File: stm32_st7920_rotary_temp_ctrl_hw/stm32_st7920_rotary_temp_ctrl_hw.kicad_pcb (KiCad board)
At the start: 2 copper layers, 100 x 100 mm, 177 parts, among them J1 Conn_01x02, J2 CONN_01X04, J3 USB_OTG, J4 CONN_01X04, J5 Conn_01x05, J7 Conn_01x03, J8 Conn_01x02, J9 Conn_01x06, Q1 C1815, Q10 C1815, Q11 IRF3205, Q12 ME15N10, Q13 ME15N10, Q14 ME15N10, Q15 ME15N10, Q2 C1815, Q3 C1815, Q4 C1815, Q5 C1815, Q6 A1015, Q7 C1815, Q8 C1815, Q9 C1815, SW1 SW_Push, SW2 SW_Push, SW3 SW_Push, SW4 SW_Push, U1 ASM1117, U10 24LC64, U2 MC34063, U3 MAX485, U4 STM32F103C8, U5 PC817, U6 74HC245, U7 PC817, U8 PC817, U9 PC817, Y1 Crystal, Y2 Crystal_GND3

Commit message: Delete block buton, Modify block connecter, Modify Block Power input, Update ALL footprint
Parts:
- removed C35, C36: 100nF, Capacitors_SMD:C_0805_HandSoldering
- removed C37: 100nF, Capacitor_SMD:C_0805_2012Metric_Pad1.15x1.40mm_HandSolder
- removed C38: 10uF, Capacitor_SMD:C_1206_3216Metric_Pad1.42x1.75mm_HandSolder
- removed D14, D15: D_Zener, nhantt-kicad-lib:SOD-80
- removed D16: SS54, nhantt-kicad-lib:D_SMB_Handsoldering
- removed D17, D18, D19, D20: FR107, nhantt-kicad-lib:D_SMA_Standard
- removed D21: TVS, nhantt-kicad-lib:D_SMA_Standard
- removed DHT1: DHT11, nhantt-kicad-lib:DHT11
- removed IoT-ETech: Val**, nhantt-kicad-lib:logo
- removed IoT-ETech: Val**, nhantt-kicad-lib:logo-Miror
- removed the J1 at (94.0, 63.5)
- removed J3: USB_OTG, nhantt-kicad-lib:USB_Micro-B
- removed J4: CONN_01X04, nhantt-kicad-lib:Header-4pin-2.54
- removed J7: Conn_01x03, nhantt-kicad-lib:Header-3pin-2.54
- removed LCD_ST7920: ST7920, nhantt-kicad-lib:ST7920
- removed Q10: C1815, nhantt-kicad-lib:SOT-23
- removed Q11: IRF3205, nhantt-kicad-lib:TO-263-2Lead
- removed Q12, Q13, Q14, Q15: ME15N10, nhantt-kicad-lib:TO-252-2
- removed R42: 1k, Resistors_SMD:R_0805_HandSoldering
- removed R43, R45, R46, R47, R48, R49, R50, R51, R52, R53: 2.2k, Resistors_SMD:R_0805_HandSoldering
- removed R44, R54, R55, R56, R57, R58, R59, R60, R61, R62: 10k, Resistors_SMD:R_0805_HandSoldering
- removed R63, R64, R65, R66, R67: 10R, Resistors_SMD:R_0805_HandSoldering
- removed SW1, SW2, SW3, SW4: SW_Push, Buttons_Switches_THT:SW_PUSH-12mm_Wuerth-430476085716
- removed U10: 24LC64, nhantt-kicad-lib:SOIC-8_3.9x4.9mm_Pitch1.27mm
- removed U6: 74HC245, Package_SO:TSSOP-20_4.4x6.5mm_P0.65mm
- removed U7, U8, U9: PC817, nhantt-kicad-lib:Optocoupler_SMD
- added F2: Fuse, Fuse:Fuse_1812_4532Metric_Pad1.30x3.40mm_HandSolder, F.Cu at (262.1, 94.8)
- added F3: Fuse, Fuse:Fuse_1812_4532Metric_Pad1.30x3.40mm_HandSolder, F.Cu at (262.1, 99.7)
- added H1: ~, Lib_Hien:KF142_9P_5.08, F.Cu at (258.1, 51.1)
- added H2: ~, Lib_Hien:KF142_9P_5.08, F.Cu at (258.1, 66.5)
- added IC1: MAX6675, Lib_Hien:MAX6675, F.Cu at (287.9, 106.0)
- added J1: USB_C_Receptacle_USB2.0, Connector_USB:USB_C_Receptacle_GCT_USB4105-xx-A_16P_TopMnt_Horizontal, F.Cu at (277.6, 106.7)
- added J1: Conn_01x02, nhantt-kicad-lib:TerminalBlock_WAGO-236_2Stift_R5mm_2pol, B.Cu at (-111.3, 64.2)
- added L3: L_Small, Resistor_SMD:R_0805_2012Metric_Pad1.20x1.40mm_HandSolder, F.Cu at (299.8, 33.0)
- added R35: 2.2k, Resistor_SMD:R_0805_2012Metric_Pad1.20x1.40mm_HandSolder, F.Cu at (251.3, 89.4)
- added R36: 20k, Resistor_SMD:R_0805_2012Metric_Pad1.20x1.40mm_HandSolder, F.Cu at (251.3, 92.3)
- added REF**: Vit-4mm, nhantt-kicad-lib:Vit-4mm, F.Cu at (-112.2, 33.7)
- added REF**: Vit-4mm, nhantt-kicad-lib:Vit-4mm, F.Cu at (-112.2, 127.7)
- added REF**: Vit-4mm, nhantt-kicad-lib:Vit-4mm, F.Cu at (-18.2, 127.7)
- added REF**: Vit-4mm, nhantt-kicad-lib:Vit-4mm, F.Cu at (-18.2, 33.7)
- added Re1: 2.2k, Resistor_SMD:R_0805_2012Metric_Pad1.20x1.40mm_HandSolder, F.Cu at (256.1, 83.5)
- added ST1: ST7920, Lib_Hien:GLCD-ST7920, F.Cu at (95.7, 104.7)
- added V1: VIT-M3, Lib_Hien:VIT-M3, F.Cu at (195.6, 34.6)
- added V2: VIT-M3, Lib_Hien:VIT-M3, F.Cu at (195.6, 49.1)
- added V3: VIT-M3, Lib_Hien:VIT-M3, F.Cu at (195.6, 56.1)
- added V4: VIT-M3, Lib_Hien:VIT-M3, F.Cu at (195.6, 63.1)
- BT1: value 3V3 -> CR1220; footprint nhantt-kicad-lib:BT3V3 -> Lib_Hien:CR1220; moved to F.Cu
- C1: value 100nF -> 100uF; footprint Capacitors_SMD:C_0805_HandSoldering -> Capacitor_SMD:CP_Elec_8x10.5; moved to F.Cu
- C10: value 1uF -> 180uF_35v; footprint Capacitors_SMD:C_0805_HandSoldering -> Capacitor_SMD:CP_Elec_6.3x9.9; moved to F.Cu
- C11, C12, C13, C14, C17, C18, C19, C20, C24, C28, C29, C3, C32, C33, C34, C4, C9: footprint Capacitors_SMD:C_0805_HandSoldering -> Capacitor_SMD:C_0805_2012Metric_Pad1.18x1.45mm_HandSolder; moved to F.Cu
- C15, C16: value 100nF -> 22pF; footprint Capacitors_SMD:C_0805_HandSoldering -> Capacitor_SMD:C_0805_2012Metric_Pad1.18x1.45mm_HandSolder; moved to F.Cu
- C2: value 100uF -> 10uF; footprint nhantt-kicad-lib:CP_Elec_8x10.5 -> Capacitor_SMD:C_0805_2012Metric_Pad1.18x1.45mm_HandSolder; moved to F.Cu
- C21, C22, C30, C31: value 100nF -> 10uF; footprint Capacitors_SMD:C_0805_HandSoldering -> Capacitor_SMD:C_0805_2012Metric_Pad1.18x1.45mm_HandSolder; moved to F.Cu
- C23, C25: value 10uF -> 100nF; footprint Capacitors_SMD:C_1206_HandSoldering -> Capacitor_SMD:C_0805_2012Metric_Pad1.18x1.45mm_HandSolder; moved to F.Cu
- C26: value 22pF -> 10uF; footprint Capacitors_SMD:C_0805_HandSoldering -> Capacitor_SMD:C_0805_2012Metric_Pad1.18x1.45mm_HandSolder; moved to F.Cu
- C27: value 22pF -> 1uF; footprint Capacitors_SMD:C_0805_HandSoldering -> Capacitor_SMD:C_0805_2012Metric_Pad1.18x1.45mm_HandSolder; moved to F.Cu
- C5: value 47uF -> 1uF_50V; footprint Capacitors_Tantalum_SMD:CP_Tantalum_Case-C_EIA-6032-28_Reflow -> Capacitor_SMD:C_0805_2012Metric_Pad1.18x1.45mm_HandSolder; moved to F.Cu
- C6: value 100nF -> 220uF_50V; footprint Capacitors_SMD:C_0805_HandSoldering -> Capacitor_SMD:CP_Elec_8x10.5; moved to F.Cu
- C7: value 100uF -> 100nF; footprint nhantt-kicad-lib:CP_Elec_8x10 -> Capacitor_SMD:C_0805_2012Metric_Pad1.18x1.45mm_HandSolder; moved to F.Cu
- C8: value 33p -> 100nF; footprint Capacitors_SMD:C_0805_HandSoldering -> Capacitor_SMD:C_0805_2012Metric_Pad1.18x1.45mm_HandSolder; moved to F.Cu
- D1: value D_ALT -> TVS; footprint nhantt-kicad-lib:D_SMA_Standard -> Diode_SMD:D_SMB; moved to F.Cu
- D10, D9: value D_Zener -> FR107; footprint nhantt-kicad-lib:SOD-80 -> Diode_SMD:D_SMA; moved to F.Cu
- D11: value D_Zener -> D; footprint nhantt-kicad-lib:SOD-80 -> Diode_SMD:D_SOD-323F; moved to F.Cu
- D12, D13: value D_Zener -> D_TVS; footprint nhantt-kicad-lib:SOD-80 -> Diode_SMD:D_SMC
- D2: value LED -> 1N4148; footprint LEDs:LED_0805 -> Diode_SMD:D_SMA; moved to F.Cu
- D3: value D_Schottky -> 1N4007_T7; footprint nhantt-kicad-lib:D_SMB_Handsoldering -> Diode_SMD:D_SOD-123F; moved to F.Cu
- D4: value D_ALT -> 1N5820; footprint nhantt-kicad-lib:SOD-80 -> Diode_SMD:D_SMA; moved to F.Cu
- D5, D8: value D_Zener -> LED; footprint nhantt-kicad-lib:SOD-80 -> LED_SMD:LED_0805_2012Metric_Pad1.15x1.40mm_HandSolder; moved to F.Cu
- D6: value LED -> D_Zener; footprint LEDs:LED_0805 -> Diode_SMD:D_SC-80_HandSoldering; moved to F.Cu
- D7: value D -> D_Zener; footprint nhantt-kicad-lib:D_SOD-323F -> Diode_SMD:D_SC-80_HandSoldering; moved to F.Cu
- F1: footprint nhantt-kicad-lib:Fuse_SMD1812 -> Fuse:Fuse_1812_4532Metric_Pad1.30x3.40mm_HandSolder; moved to F.Cu
- J2: footprint nhantt-kicad-lib:Header-4pin-2.54 -> Connector_PinHeader_2.54mm:PinHeader_1x04_P2.54mm_Vertical; moved to F.Cu
- L1: value L -> L_Ferrite; footprint nhantt-kicad-lib:Inductor_5.2x5.8x4.5 -> Inductor_THT:L_Radial_D7.5mm_P3.50mm_Fastron_07P; moved to F.Cu
- L2: value L_Small -> 68uH_2A; footprint Resistors_SMD:R_0805_HandSoldering -> Inductor_SMD:L_Bourns-SRU8028_8.0x8.0mm; moved to F.Cu
- LS1: moved to F.Cu
- Q1, Q2, Q3, Q7, Q8, Q9: footprint nhantt-kicad-lib:SOT-23 -> Package_TO_SOT_SMD:SOT-23; moved to F.Cu
- Q4, Q5: value C1815 -> ME15N10; footprint nhantt-kicad-lib:SOT-23 -> Package_TO_SOT_SMD:TO-252-2; moved to F.Cu
- Q6: value A1015 -> C1815; footprint nhantt-kicad-lib:SOT-23 -> Package_TO_SOT_SMD:SOT-23; moved to F.Cu
- R1: value 0.15 -> 10k; footprint Resistors_SMD:R_1206_HandSoldering -> Resistor_SMD:R_0805_2012Metric_Pad1.20x1.40mm_HandSolder; moved to F.Cu
- R10: value 1.5k -> 4.7K; footprint Resistors_SMD:R_0805_HandSoldering -> Resistor_SMD:R_0805_2012Metric_Pad1.20x1.40mm_HandSolder; moved to F.Cu
- R11, R20: value 4.7k -> 10k; footprint Resistors_SMD:R_0805_HandSoldering -> Resistor_SMD:R_0805_2012Metric_Pad1.20x1.40mm_HandSolder; moved to F.Cu
- R12: value 2.2k -> 10k; footprint Resistors_SMD:R_0805_HandSoldering -> Resistor_SMD:R_0805_2012Metric_Pad1.20x1.40mm_HandSolder; moved to F.Cu
- R13: value 10k -> 10K; footprint Resistors_SMD:R_0805_HandSoldering -> Resistor_SMD:R_0805_2012Metric_Pad1.20x1.40mm_HandSolder; moved to F.Cu
- R14: value 22R -> 10K; footprint Resistors_SMD:R_0805_HandSoldering -> Resistor_SMD:R_0805_2012Metric_Pad1.20x1.40mm_HandSolder; moved to F.Cu
- R15: value 2.2k -> 10K; footprint Resistors_SMD:R_0805_HandSoldering -> Resistor_SMD:R_0805_2012Metric_Pad1.20x1.40mm_HandSolder; moved to F.Cu
- R16: value 20k -> 1k; footprint Resistors_SMD:R_0805_HandSoldering -> Resistor_SMD:R_0805_2012Metric_Pad1.20x1.40mm_HandSolder; moved to F.Cu
- R17: value 22R -> 2.2k; footprint Resistors_SMD:R_0805_HandSoldering -> Resistor_SMD:R_0805_2012Metric_Pad1.20x1.40mm_HandSolder; moved to F.Cu
- R18, R32, R34: value 10k -> 2.2k; footprint Resistors_SMD:R_0805_HandSoldering -> Resistor_SMD:R_0805_2012Metric_Pad1.20x1.40mm_HandSolder; moved to F.Cu
- R19: value 4.7k -> 2.2k; footprint Resistors_SMD:R_0805_HandSoldering -> Resistor_SMD:R_0805_2012Metric_Pad1.20x1.40mm_HandSolder; moved to F.Cu
- R2: value 1k -> 220R; footprint Resistors_SMD:R_0805_HandSoldering -> Resistor_SMD:R_0805_2012Metric_Pad1.20x1.40mm_HandSolder; moved to F.Cu
- R21, R25, R30, R39, R41: value 1k -> 10k; footprint Resistors_SMD:R_0805_HandSoldering -> Resistor_SMD:R_0805_2012Metric_Pad1.20x1.40mm_HandSolder; moved to F.Cu
- R22: value 2.2k -> 1k; footprint Resistors_SMD:R_0805_HandSoldering -> Resistor_SMD:R_0805_2012Metric_Pad1.20x1.40mm_HandSolder; moved to F.Cu
- R23, R24, R37: footprint Resistors_SMD:R_0805_HandSoldering -> Resistor_SMD:R_0805_2012Metric_Pad1.20x1.40mm_HandSolder; moved to F.Cu
- R26, R27: value 4.7k -> 10R; footprint Resistors_SMD:R_0805_HandSoldering -> Resistor_SMD:R_0805_2012Metric_Pad1.20x1.40mm_HandSolder; moved to F.Cu
- R28: value 0R -> 2.2k; footprint Resistors_SMD:R_0805_HandSoldering -> Resistor_SMD:R_0805_2012Metric_Pad1.20x1.40mm_HandSolder; moved to F.Cu
- R29: value 0R -> 4.7k; footprint Resistors_SMD:R_0805_HandSoldering -> Resistor_SMD:R_0805_2012Metric_Pad1.20x1.40mm_HandSolder; moved to F.Cu
- R3: value 3k -> 2.2k; footprint Resistors_SMD:R_0805_HandSoldering -> Resistor_SMD:R_0805_2012Metric_Pad1.20x1.40mm_HandSolder; moved to F.Cu
- R31: value 220R -> 10k; footprint Resistors_SMD:R_0805_HandSoldering -> Resistor_SMD:R_0805_2012Metric_Pad1.20x1.40mm_HandSolder; moved to F.Cu
- R33, R40: value 1k -> 2.2k; footprint Resistors_SMD:R_0805_HandSoldering -> Resistor_SMD:R_0805_2012Metric_Pad1.20x1.40mm_HandSolder; moved to F.Cu
- R38: value 1k -> 20k; footprint Resistors_SMD:R_0805_HandSoldering -> Resistor_SMD:R_0805_2012Metric_Pad1.20x1.40mm_HandSolder; moved to F.Cu
- R4: value 1k -> 5.1K; footprint Resistors_SMD:R_0805_HandSoldering -> Resistor_SMD:R_0805_2012Metric_Pad1.20x1.40mm_HandSolder; moved to F.Cu
- R5: value 10k -> 5.1K; footprint Resistors_SMD:R_0805_HandSoldering -> Resistor_SMD:R_0805_2012Metric_Pad1.20x1.40mm_HandSolder; moved to F.Cu
- R6: value 10k -> 22R; footprint Resistors_SMD:R_0805_HandSoldering -> Resistor_SMD:R_0805_2012Metric_Pad1.20x1.40mm_HandSolder; moved to F.Cu
- R7: value 20k -> 22R; footprint Resistors_SMD:R_0805_HandSoldering -> Resistor_SMD:R_0805_2012Metric_Pad1.20x1.40mm_HandSolder; moved to F.Cu
- R8: value 10k -> 1.5k; footprint Resistors_SMD:R_0805_HandSoldering -> Resistor_SMD:R_0805_2012Metric_Pad1.20x1.40mm_HandSolder; moved to F.Cu
- R9: value 10k -> 4.7K; footprint Resistors_SMD:R_0805_HandSoldering -> Resistor_SMD:R_0805_2012Metric_Pad1.20x1.40mm_HandSolder; moved to F.Cu
- RV1: value 100k -> 100K; footprint nhantt-kicad-lib:VR-3362P -> Potentiometer_SMD:Potentiometer_ACP_CA14-VSMD_Vertical_Hole; moved to F.Cu
- U1: value ASM1117 -> XL1509; footprint nhantt-kicad-lib:SOT-223 -> Package_SO:SOIC-8-1EP_3.9x4.9mm_P1.27mm_EP2.41x3.81mm; moved to F.Cu
- U2: value MC34063 -> 74HC245; footprint nhantt-kicad-lib:SOIC-8_3.9x4.9mm_Pitch1.27mm -> Package_SO:HTSSOP-20-1EP_4.4x6.5mm_P0.65mm_EP2.74x3.86mm; moved to F.Cu
- U3: value MAX485 -> STM32F103C8; footprint nhantt-kicad-lib:SOIC-8_3.9x4.9mm_Pitch1.27mm -> Package_QFP:LQFP-48-1EP_7x7mm_P0.5mm_EP3.6x3.6mm_ThermalVias; moved to F.Cu
- U4: value STM32F103C8 -> ASM1117; footprint nhantt-kicad-lib:LQFP-48_7x7mm_Pitch0.5mm -> Package_TO_SOT_SMD:SOT-223; moved to F.Cu
- U5: value PC817 -> MAX485; footprint nhantt-kicad-lib:Optocoupler_SMD -> Package_SO:SO-8_3.9x4.9mm_P1.27mm; moved to F.Cu
- Y1: value Crystal -> 8MHz; footprint nhantt-kicad-lib:Crystal_SMD_HC49-SD -> Crystal:Crystal_SMD_5032-2Pin_5.0x3.2mm_HandSoldering; moved to F.Cu
- Y2: value Crystal_GND3 -> 32,768KHz; footprint nhantt-kicad-lib:Crystal_Round_Horizontal_3mm_smd -> Crystal:Crystal_DS15_D1.5mm_L5.0mm_Horizontal; moved to F.Cu
- moved J5 205.3 mm to (-111.3, 77.7)
- moved J8 205.2 mm to (-111.2, 50.7)
- moved J9 205.2 mm to (-19.2, 70.7)
- moved D8 204.0 mm to (309.3, 58.4)
- moved D5 203.7 mm to (309.3, 55.4)
- moved D1 202.2 mm to (311.1, 62.7), turned to 0 degrees
- moved Q3 200.1 mm to (293.8, 43.2), turned to 0 degrees
- moved U3 199.9 mm to (309.4, 106.5), turned to 0 degrees
- moved U2 186.9 mm to (310.5, 49.6), turned to 0 degrees
- moved C8 182.3 mm to (287.1, 119.4)
- moved C29 181.7 mm to (293.4, 68.7), turned to 0 degrees
- moved Q2 179.9 mm to (289.7, 33.0), turned to 0 degrees
- moved L1 175.6 mm to (307.1, 41.0), turned to 0 degrees
- moved D3 174.7 mm to (298.6, 103.1)
- moved C33 171.5 mm to (293.4, 80.8), turned to 0 degrees
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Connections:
- BT1 pad 1: Net-(BT1-Pad1) -> Net-(BT1-+)
- C10 pad 1: GND -> +5V
- C10 pad 2: Net-(C10-Pad2) -> GND
- C11 pad 1: GND -> +5V
- C11 pad 2: Net-(C10-Pad2) -> GND
- C12 pad 1: Net-(C12-Pad1) -> +3V3
- C13 pad 1: Net-(BT1-Pad1) -> Net-(BT1-+)
- C14 pad 1: /BT4 -> Net-(U3-~{NRST})
- C15 pad 1: +5V -> GND
- C15 pad 2: GND -> /OSC32I
- C16 pad 1: +3V3 -> GND
- C16 pad 2: GND -> /OSC32O
- C2 pad 1: +24V -> +5V
- C23 pad 1: +3V3 -> /ROTORY_B
- C24 pad 1: GND -> +3V3
- C24 pad 2: /input1 -> GND
- C25 pad 1: +5V -> /ROTORY_A
- C26 pad 1: GND -> +3V3
- C26 pad 2: /OSC32I -> GND
- C27 pad 2: /OSC32O -> Net-(U3-VDDA)
- C28 pad 2: +5V -> Net-(U3-VDDA)
- C29 pad 1: /BT1 -> +3V3
- C3 pad 1: /BT2 -> GND
- C3 pad 2: GND -> +5V
- C30 pad 1: GND -> +5V
- C30 pad 2: +5V -> GND
- C31 pad 1: GND -> +3V3
- C31 pad 2: /input2 -> GND
- C32 pad 1: GND -> +5V
- C32 pad 2: /input3 -> GND
- C33 pad 1: GND -> /SW_Rotory
- C33 pad 2: /input4 -> GND
- C34 pad 1: +3V3 -> GND
- C34 pad 2: GND -> +5V
- C4 pad 1: +3V3 -> +24V
- C5 pad 1: +3V3 -> +24V
- C6 pad 1: +5V -> Net-(U1-Vi)
- C7 pad 1: +5V -> Net-(U1-Vi)
- C8 pad 1: Net-(C8-Pad1) -> +5V
- C9 pad 1: /BT3 -> +5V
- D1 pad 1: +24V -> Net-(D2-A)
- D1 pad 2: Net-(D1-Pad2) -> GND
- D10 pad 1: /IN4 -> +24V
- D10 pad 2: Net-(D10-Pad2) -> /PWM_Servo
- D11 pad 1: Net-(D11-Pad1) -> +5V
- D11 pad 2: GND -> Net-(D11-A)
- D12 pad 1: Net-(D12-Pad1) -> Net-(D12-A1)
- D13 pad 1: Net-(D13-Pad1) -> GND
- D13 pad 2: GND -> Net-(D13-A2)
- D2 pad 1: GND -> +24V
- D2 pad 2: Net-(D2-Pad2) -> Net-(D2-A)
- D3 pad 1: Net-(D3-Pad1) -> +5V
- D3 pad 2: GND -> Net-(D3-A)
- D4 pad 1: +5V -> Net-(D4-K)
- D4 pad 2: Net-(D4-Pad2) -> GND
- D5 pad 1: /IN1 -> GND
- D5 pad 2: Net-(D5-Pad2) -> Net-(D5-A)
- D6 pad 1: /LED_STT -> Net-(D6-K)
- D6 pad 2: Net-(D6-Pad2) -> GND
- D7 pad 1: +5V -> Net-(D7-K)
- D7 pad 2: Net-(D7-Pad2) -> GND
- D8 pad 1: /IN2 -> /LED_STT
- D8 pad 2: Net-(D8-Pad2) -> Net-(D8-A)
- D9 pad 1: /IN3 -> +24V
- D9 pad 2: Net-(D9-Pad2) -> /PWM_Heater
- F1 pad 2: Net-(D1-Pad2) -> Net-(D2-A)
- J2 pad 3: Net-(J2-Pad3) -> /SWDIO
- J2 pad 4: Net-(J2-Pad4) -> /SWCLK
- L1 pad 1: +5V -> +24V
- L1 pad 2: Net-(D3-Pad1) -> Net-(U1-Vi)
- L2 pad 1: +3V3 -> Net-(D4-K)
- L2 pad 2: Net-(C10-Pad2) -> +5V
- LS1 pad 2: Net-(D7-Pad2) -> Net-(D11-A)
- Q1 pad 1: Net-(Q1-Pad1) -> Net-(Q1-B)
- Q1 pad 3: Net-(D7-Pad2) -> Net-(Q1-C)
- Q2 pad 1: Net-(Q2-Pad1) -> Net-(Q2-B)
- Q2 pad 3: Net-(Q2-Pad3) -> Net-(D6-K)
- Q3 pad 1: Net-(Q3-Pad1) -> Net-(Q3-B)
- Q3 pad 3: Net-(Q3-Pad3) -> Net-(D7-K)
- Q4 pad 1: Net-(Q4-Pad1) -> Net-(Q4-G)
- Q4 pad 2: GND -> /PWM_Heater
- Q4 pad 3: Net-(Q4-Pad3) -> GND
- Q5 pad 1: Net-(Q5-Pad1) -> Net-(Q5-G)
- Q5 pad 2: Net-(D11-Pad1) -> /PWM_Servo
- Q5 pad 3: Net-(Q5-Pad3) -> GND
- Q6 pad 1: Net-(Q5-Pad1) -> Net-(Q6-B)
- Q6 pad 2: Net-(D11-Pad1) -> GND
- Q6 pad 3: GND -> Net-(Q6-C)
- Q7 pad 1: Net-(Q7-Pad1) -> Net-(Q7-B)
- Q7 pad 3: Net-(D12-Pad1) -> Net-(D11-A)
- Q8 pad 1: Net-(Q8-Pad1) -> Net-(Q8-B)
- Q8 pad 3: Net-(D13-Pad1) -> /ENA_Servo
- Q9 pad 3: Net-(D14-Pad1) -> /DIR_Servo
- R1 pad 1: Net-(R1-Pad1) -> Net-(ST1-PSB)
- R1 pad 2: +24V -> GND
- R10 pad 1: /USB_DIS -> /I2C1_SCL
- R10 pad 2: Net-(J3-Pad3) -> +3V3
- R11 pad 1: /485_RX -> +3V3
- R11 pad 2: Net-(R11-Pad2) -> Net-(U3-~{NRST})
- R12 pad 1: /A -> Net-(U3-BOOT0)
- R12 pad 2: /B -> GND
- R13 pad 1: /485_RX -> /ROTORY_B
- R13 pad 2: GND -> +3V3
- R14 pad 1: /USBDP -> /ROTORY_A
- R14 pad 2: Net-(J3-Pad3) -> +3V3
- R15 pad 1: /485_TX -> /SW_Rotory
- R15 pad 2: Net-(Q2-Pad1) -> +3V3
- R16 pad 1: /B -> Net-(D5-A)
- R16 pad 2: GND -> +5V
- R17 pad 1: /USBDM -> /PWM_1
- R17 pad 2: Net-(J3-Pad2) -> +3V3
- R18 pad 1: /BT2 -> Net-(Q2-B)
- R18 pad 2: +3V3 -> /PWM_1
- R19 pad 1: /SDA -> Net-(Q3-B)
- R19 pad 2: +3V3 -> /PWM_2
- R2 pad 1: Net-(D2-Pad2) -> Net-(ST1-BLK)
- R2 pad 2: +5V -> Net-(Q1-C)
- R20 pad 1: /SCL -> Net-(D6-K)
- R20 pad 2: +3V3 -> +24V
- R21 pad 1: Net-(R21-Pad1) -> Net-(D7-K)
- R21 pad 2: Net-(D5-Pad2) -> +24V
- R22 pad 1: /Buzzer -> Net-(D8-A)
- R22 pad 2: Net-(Q1-Pad1) -> +3V3
- R23 pad 1: /BT3 -> /485_RX
- R23 pad 2: +3V3 -> GND
- R24 pad 1: /BT4 -> GND
- R24 pad 2: +3V3 -> Net-(D6-K)
- R25 pad 1: /input1 -> GND
- R25 pad 2: +3V3 -> Net-(D7-K)
- R26 pad 1: /DHT11 -> Net-(D6-K)
- R26 pad 2: +3V3 -> Net-(Q4-G)
- R27 pad 1: /DS18B20 -> Net-(D7-K)
- R27 pad 2: +3V3 -> Net-(Q5-G)
- R28 pad 1: /I/O2 -> /485_TX
- R28 pad 2: Net-(J2-Pad3) -> Net-(Q6-B)
- R29 pad 1: /I/O1 -> /485_RX
- R29 pad 2: Net-(J2-Pad4) -> Net-(U5-RO)
- R3 pad 1: Net-(R3-Pad1) -> /LCD_BL
- R3 pad 2: +5V -> Net-(Q1-B)
- R30 pad 1: Net-(D6-Pad2) -> +5V
- R30 pad 2: +3V3 -> Net-(Q6-C)
- R31 pad 1: Net-(R31-Pad1) -> +5V
- R31 pad 2: Net-(Q3-Pad3) -> Net-(U5-RO)
- R32 pad 1: /BT1 -> /CTR_DIR
- R33 pad 1: Net-(R33-Pad1) -> /CTR_ENA
- R33 pad 2: Net-(D8-Pad2) -> +3V3
- R34 pad 1: Net-(R34-Pad1) -> Net-(Q8-B)
- R34 pad 2: GND -> /CTR_DIR
- R37 pad 1: /LCD_BL -> Net-(D12-A1)
- R37 pad 2: Net-(Q3-Pad1) -> Net-(D13-A2)
- R38 pad 1: /input2 -> Net-(D13-A2)
- R38 pad 2: +3V3 -> GND
- R39 pad 1: Net-(R39-Pad1) -> /ENA_Servo
- R39 pad 2: Net-(D9-Pad2) -> +24V
- R4 pad 2: Net-(R3-Pad1) -> Net-(J1-CC1)
- R40 pad 1: /input3 -> /BUZZER
- R40 pad 2: +3V3 -> Net-(Q7-B)
- R41 pad 1: Net-(R41-Pad1) -> /DIR_Servo
- R41 pad 2: Net-(D10-Pad2) -> +24V
- R5 pad 1: +3V3 -> GND
- R5 pad 2: Net-(C12-Pad1) -> Net-(J1-CC2)
- R6 pad 1: Net-(R6-Pad1) -> /USBDM
- R6 pad 2: GND -> Net-(J1-D--PadA7)
- R7 pad 1: +5V -> /USBDP
- R7 pad 2: /A -> Net-(J1-D+-PadA6)
- R8 pad 1: +5V -> /USB_DIS
- R8 pad 2: Net-(R11-Pad2) -> Net-(J1-D+-PadA6)
- R9 pad 1: +5V -> /I2C1_SDA
- R9 pad 2: Net-(Q2-Pad3) -> +3V3
- RV1 pad 1: GND -> +5V
- RV1 pad 3: +5V -> GND
- U1 pad 1: GND -> Net-(U1-Vi)
- U1 pad 2: +3V3 -> Net-(D4-K)
- U1 pad 4: +3V3 -> GND
- U2 pad 1: Net-(R1-Pad1) -> +5V
- U2 pad 2: Net-(D3-Pad1) -> /SPI1_LCD_CS
- U2 pad 3: Net-(C8-Pad1) -> /SPI1_CLK
- U2 pad 4: GND -> /SPI1_MOSI
- U2 pad 5: Net-(R3-Pad1) -> /SPI1_LCD_RST
- U2 pad 6: +24V -> /SPI1_LCD_BL
- U2 pad 7: Net-(R1-Pad1) -> unconnected-(U2-A5-Pad7)
- U2 pad 8: Net-(R1-Pad1) -> unconnected-(U2-A6-Pad8)
- U3 pad 1: Net-(R11-Pad2) -> Net-(BT1-+)
- U3 pad 2: Net-(Q2-Pad3) -> /LED_STT
- U3 pad 3: Net-(Q2-Pad3) -> /OSC32I
- U3 pad 4: GND -> /OSC32O
- U3 pad 5: GND -> /OSCI
- U3 pad 6: /A -> /OSCO
- U3 pad 7: /B -> Net-(U3-~{NRST})
- U3 pad 8: +5V -> GND
- U4 pad 1: Net-(BT1-Pad1) -> GND
- U4 pad 2: /LED_STT -> +3V3
- U4 pad 3: /OSC32I -> +5V
- U4 pad 4: /OSC32O -> +3V3
- U5 pad 1: Net-(R21-Pad1) -> Net-(U5-RO)
- U5 pad 2: GND -> Net-(Q6-C)
- U5 pad 3: GND -> Net-(Q6-C)
- U5 pad 4: /input1 -> GND
- Y2 pad 1: /OSC32O -> /OSC32I
- Y2 pad 2: /OSC32I -> /OSC32O
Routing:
- net GND: track 992.2 -> 0.00 mm, vias 289 -> 0
- net +5V: track 362.3 -> 0.00 mm, vias 32 -> 0
- net +3V3: track 361.6 -> 0.00 mm, vias 27 -> 0
- net +24V: track 259.9 -> 0.00 mm, vias 32 -> 0
- net /BT1: track 112.6 -> 0.00 mm, vias 3 -> 0
- net /BT2: track 94.3 -> 0.00 mm, vias 3 -> 0
- net /BT4: track 88.0 -> 0.00 mm, vias 2 -> 0
- net /BT3: track 85.1 -> 0.00 mm, vias 3 -> 0
- net /DHT11: track 80.3 -> 0.00 mm, vias 3 -> 0
- net /ctrl1: track 63.7 -> 0.00 mm, vias 2 -> 0
- net /USB_DIS: track 55.5 -> 0.00 mm, vias 2 -> 0
- net /ctrl3: track 54.5 -> 0.00 mm, vias 2 -> 0
- net /OUT1: track 54.2 -> 0.00 mm
- net /USBDM: track 52.1 -> 0.00 mm, vias 2 -> 0
- net /USBDP: track 51.9 -> 0.00 mm, vias 2 -> 0
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- removed copper zone on B.Cu, net +24V
- removed copper zone on B.Cu, net +3V3
- removed copper zone on B.Cu, net +5V
- removed copper zone on F.Cu, net +5V
- removed copper zone on F.Cu, net /OUT1
- removed copper zone on F.Cu, net /OUT2
- removed copper zone on F.Cu, net /OUT3
- removed copper zone on B.Cu, net /OUT4
- removed copper zone on F.Cu, net /OUT4
- removed copper zone on B.Cu, net /PWM
- removed copper zone on F.Cu, net /PWM
- removed copper zone on B.Cu, net GND
- removed copper zone on F.Cu, net GND
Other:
- board size 100 x 100 mm -> 305.2 x 100.7 mm
- board text removed: "+VIN"
- board text removed: "A"
- board text removed: "B"
- board text removed: "COM"
- board text removed: "DS18B20"
- board text removed: "EXTEND"
- board text removed: "GND"
- board text removed: "IN1"
- board text removed: "IN2"
- board text removed: "IN3"
- board text removed: "IN4"
- board text removed: "OUT1"
- board text removed: "OUT2"
- board text removed: "OUT3"
- board text removed: "OUT4"
- board text removed: "PWM"
- board text removed: "USB"
- board text removed: "V1.0"
- board text removed: "VIN"

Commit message: modify block control servo, block control heater, create button, create 3 led status
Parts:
- removed the J1 at (-111.3, 64.2)
- removed J5: Conn_01x05, nhantt-kicad-lib:TerminalBlock_WAGO-236_2Stift_R5mm_5pol
- removed J8: Conn_01x02, nhantt-kicad-lib:TerminalBlock_WAGO-236_2Stift_R5mm_2pol
- removed J9: Conn_01x06, nhantt-kicad-lib:TerminalBlock_WAGO-236_2Stift_R5mm_6pol
- removed the REF** at (-112.2, 33.7)
- removed the REF** at (-112.2, 127.7)
- removed the REF** at (-18.2, 127.7)
- removed the REF** at (-18.2, 33.7)
- added C35: 220uF_50V, Capacitor_SMD:CP_Elec_8x10.5, F.Cu at (270.4, 164.6)
- added C36: 100nF, Capacitor_SMD:C_0805_2012Metric_Pad1.18x1.45mm_HandSolder, F.Cu at (261.2, 151.9)
- added C37: 100nF, Capacitor_SMD:C_0805_2012Metric_Pad1.18x1.45mm_HandSolder, F.Cu at (261.2, 154.9)
- added C38: 100nF, Capacitor_SMD:C_0805_2012Metric_Pad1.18x1.45mm_HandSolder, F.Cu at (261.2, 157.9)
- added D14: LED, LED_THT:LED_D3.0mm, F.Cu at (279.6, 144.6)
- added D15: LED, LED_THT:LED_D3.0mm, F.Cu at (279.6, 150.2)
- added D16: LED, LED_THT:LED_D3.0mm, F.Cu at (279.6, 155.7)
- added D17: SS54, Diode_SMD:D_SMA, F.Cu at (267.8, 139.6)
- added D6: 12V, Diode_SMD:D_SMA, F.Cu at (267.8, 125.9)
- added D8: SS54, Diode_SMD:D_SMA, F.Cu at (267.8, 130.5)
- added D9: 12V, Diode_SMD:D_SMA, F.Cu at (267.8, 135.0)
- added Q10: C1815, Package_TO_SOT_SMD:SOT-23, F.Cu at (261.2, 139.2)
- added Q11: C1815, Package_TO_SOT_SMD:SOT-23, F.Cu at (261.2, 143.7)
- added Q12: C1815, Package_TO_SOT_SMD:SOT-23, F.Cu at (261.2, 148.1)
- added Q13: IRF3205, Package_TO_SOT_SMD:TO-263-2, B.Cu at (158.2, 19.1)
- added Q2: C1815, Package_TO_SOT_SMD:SOT-23, F.Cu at (261.2, 125.9)
- added Q4: C1815, Package_TO_SOT_SMD:SOT-23, F.Cu at (261.2, 130.3)
- added Q8: IRF3205, Package_TO_SOT_SMD:TO-263-2, B.Cu at (137.3, 19.4)
- added Q9: C1815, Package_TO_SOT_SMD:SOT-23, F.Cu at (261.2, 134.8)
- added R17: 2.2k, Resistor_SMD:R_0805_2012Metric_Pad1.20x1.40mm_HandSolder, F.Cu at (266.1, 143.3)
- added R18: 10K, Resistor_SMD:R_0805_2012Metric_Pad1.20x1.40mm_HandSolder, F.Cu at (266.1, 146.3)
- added R20: 2.2k, Resistor_SMD:R_0805_2012Metric_Pad1.20x1.40mm_HandSolder, F.Cu at (266.1, 149.2)
- added R22: 10K, Resistor_SMD:R_0805_2012Metric_Pad1.20x1.40mm_HandSolder, F.Cu at (266.1, 152.2)
- added R24: 10K, Resistor_SMD:R_0805_2012Metric_Pad1.20x1.40mm_HandSolder, F.Cu at (266.1, 155.1)
- added R26: 10K, Resistor_SMD:R_0805_2012Metric_Pad1.20x1.40mm_HandSolder, F.Cu at (266.1, 158.1)
- added R32: 10K, Resistor_SMD:R_0805_2012Metric_Pad1.20x1.40mm_HandSolder, F.Cu at (270.8, 143.3)
- added R33: 10K, Resistor_SMD:R_0805_2012Metric_Pad1.20x1.40mm_HandSolder, F.Cu at (270.8, 146.3)
- added R34: 1k, Resistor_SMD:R_0805_2012Metric_Pad1.20x1.40mm_HandSolder, F.Cu at (270.8, 149.2)
- added R35: 1k, Resistor_SMD:R_0805_2012Metric_Pad1.20x1.40mm_HandSolder, F.Cu at (270.8, 152.2)
- added R39: 1k, Resistor_SMD:R_0805_2012Metric_Pad1.20x1.40mm_HandSolder, F.Cu at (270.8, 155.1)
- added R41: 2.2k, Resistor_SMD:R_0805_2012Metric_Pad1.20x1.40mm_HandSolder, F.Cu at (270.8, 158.1)
- added R42: 10K, Resistor_SMD:R_0805_2012Metric_Pad1.20x1.40mm_HandSolder, F.Cu at (275.6, 143.3)
- added R43: 2.2k, Resistor_SMD:R_0805_2012Metric_Pad1.20x1.40mm_HandSolder, F.Cu at (275.6, 146.3)
- added R44: 10K, Resistor_SMD:R_0805_2012Metric_Pad1.20x1.40mm_HandSolder, F.Cu at (275.6, 149.2)
- added R45: 10K, Resistor_SMD:R_0805_2012Metric_Pad1.20x1.40mm_HandSolder, F.Cu at (275.6, 152.2)
- added R46: 10K, Resistor_SMD:R_0805_2012Metric_Pad1.20x1.40mm_HandSolder, F.Cu at (275.6, 155.1)
- added SW1: RotaryEncoder_Switch, Lib_Hien:Rotary-Encoder-SW, F.Cu at (161.4, 121.3)
- added SW2: BT_1, Lib_Hien:SW_PUSH-12.3mm, F.Cu at (128.0, 114.8)
- added SW3: BT_1, Lib_Hien:SW_PUSH-12.3mm, F.Cu at (128.1, 129.9)
- added U6: ~, Lib_Hien:ULN2803AD, F.Cu at (249.2, 157.3)
- BT1, C1, C10, C11, C12, C13, C14, C15, C16, C17, C18, C19, C2, C20, C21, C22, C23, C24, C25, C26, C27, C28, C29, C3, C30, C31, C32, C33, C34, C4, C5, C6, C7, C8, C9, D1, D10, D11, D12, D13, D2, D3, D4, D5, D6, D7, D8, D9, F1, F2, F3, H1, H2, IC1, J1, J2, L1, L2, L3, Q1, Q2, Q3, Q4, Q5, Q6, Q7, Q8, Q9, R1, R10, R11, R12, R13, R14, R15, R16, R17, R18, R19, R2, R20, R21, R22, R23, R24, R25, R26, R27, R28, R29, R3, R30, R31, R32, R33, R34, R35, R36, R37, R38, R39, R4, R40, R41, R5, R6, R7, R8, R9, Re1, U1, U2, U3, U4, U5, Y1, Y2: moved to B.Cu
- RV1: value 100K -> 100K/EVM3E-104; footprint Potentiometer_SMD:Potentiometer_ACP_CA14-VSMD_Vertical_Hole -> Lib_Hien:TRIMMER-EVM3E-104
- moved Q4 218.0 mm to (82.4, 59.7), turned to 180 degrees
- moved Q2 208.6 mm to (81.6, 47.0), turned to 180 degrees
- moved D1 206.9 mm to (105.7, 38.4), turned to -90 degrees
- moved D6 206.9 mm to (81.8, 51.3), turned to 180 degrees
- moved Q1 200.9 mm to (103.9, 104.3), turned to -90 degrees
- moved D9 196.4 mm to (81.8, 65.2), turned to 180 degrees
- moved D2 190.3 mm to (110.0, 38.2), turned to 90 degrees
- moved L1 186.9 mm to (120.3, 36.5), turned to -90 degrees
- moved IC1 181.4 mm to (109.5, 73.0), turned to 180 degrees
- moved L3 178.9 mm to (127.4, 80.6), turned to 180 degrees
- moved U3 176.6 mm to (136.5, 70.1), turned to 90 degrees
- moved F1 168.9 mm to (101.2, 38.4), turned to 90 degrees
- moved D4 168.7 mm to (131.7, 49.9), turned to -90 degrees
- moved D5 168.4 mm to (141.7, 39.0), turned to -90 degrees
- moved R26 165.2 mm to (85.1, 54.5), turned to 180 degrees
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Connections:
- H1 pad 1: unconnected-(H1-Pad1) -> VIN
- H1 pad 2: unconnected-(H1-Pad2) -> GND
- IC1 pad 5: /SPI1_CLK -> /SPI2_CLK
- IC1 pad 7: /SPI1_MISO -> /SPI2_MISO
- R19 pad 2: /PWM_2 -> /ULN_PWM_2
- Re1 pad 1: /PWM_2 -> /ULN_PWM_2
- U3 pad 16: /SPI1_MISO -> /PWM_3
- U3 pad 18: /MAX6675_CS -> /EXTRA_1
- U3 pad 2: /LED_STT -> /RED
- U3 pad 21: unconnected-(U3-PB10/I2C2_SCL/USART3_TX-Pad21) -> /BT1
- U3 pad 22: unconnected-(U3-PB11/I2C2_SDA/USART3_RX-Pad22) -> /BT2
- U3 pad 25: unconnected-(U3-PB12/SPI2_NSS/I2C2_SMBA/USART3_CK/TIM1_BKIN-Pad25) -> /MAX6675_CS
- U3 pad 26: unconnected-(U3-PB13/SPI2_SCK/USART3_CTS/TIM1_CH1N-Pad26) -> /SPI2_CLK
- U3 pad 27: /BT1 -> /SPI2_MISO
- U3 pad 28: /BT2 -> /EXTRA_2
- U3 pad 45: unconnected-(U3-PB8/TIM4_CH3-Pad45) -> /YELLOW
- U3 pad 46: unconnected-(U3-PB9/TIM4_CH4-Pad46) -> /GREEN
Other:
- board size 305.2 x 100.7 mm -> 100 x 100 mm

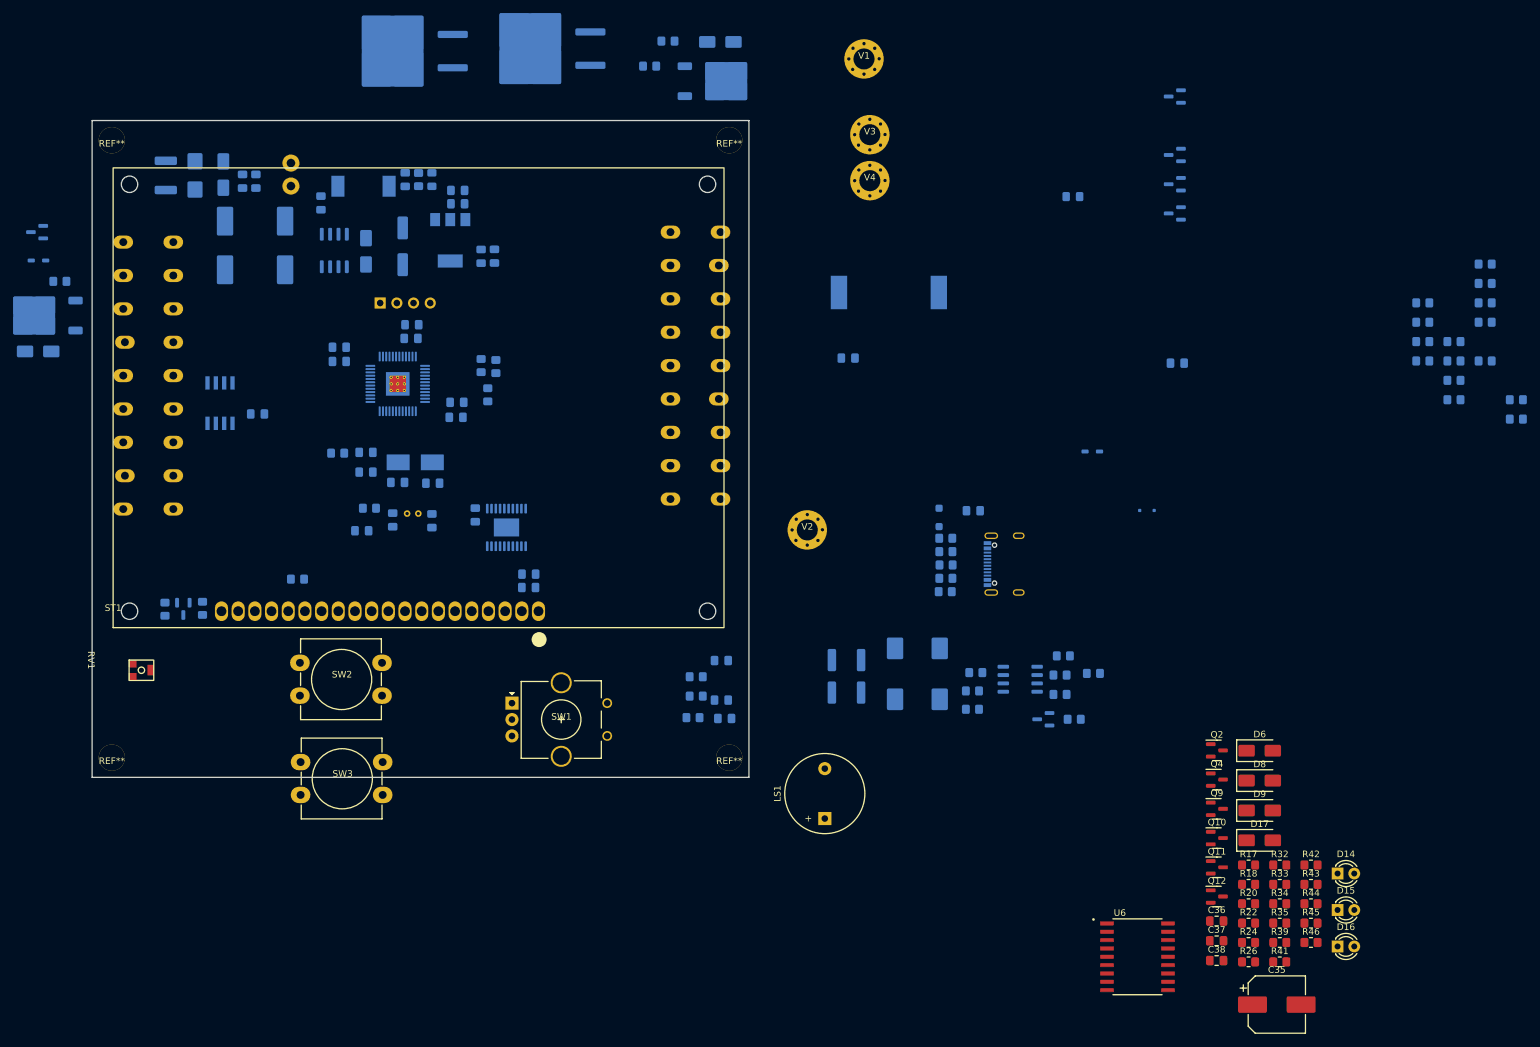
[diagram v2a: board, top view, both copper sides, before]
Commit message: Xep xong linh kien ben PCB, con mot vai output chua cho ra terminal
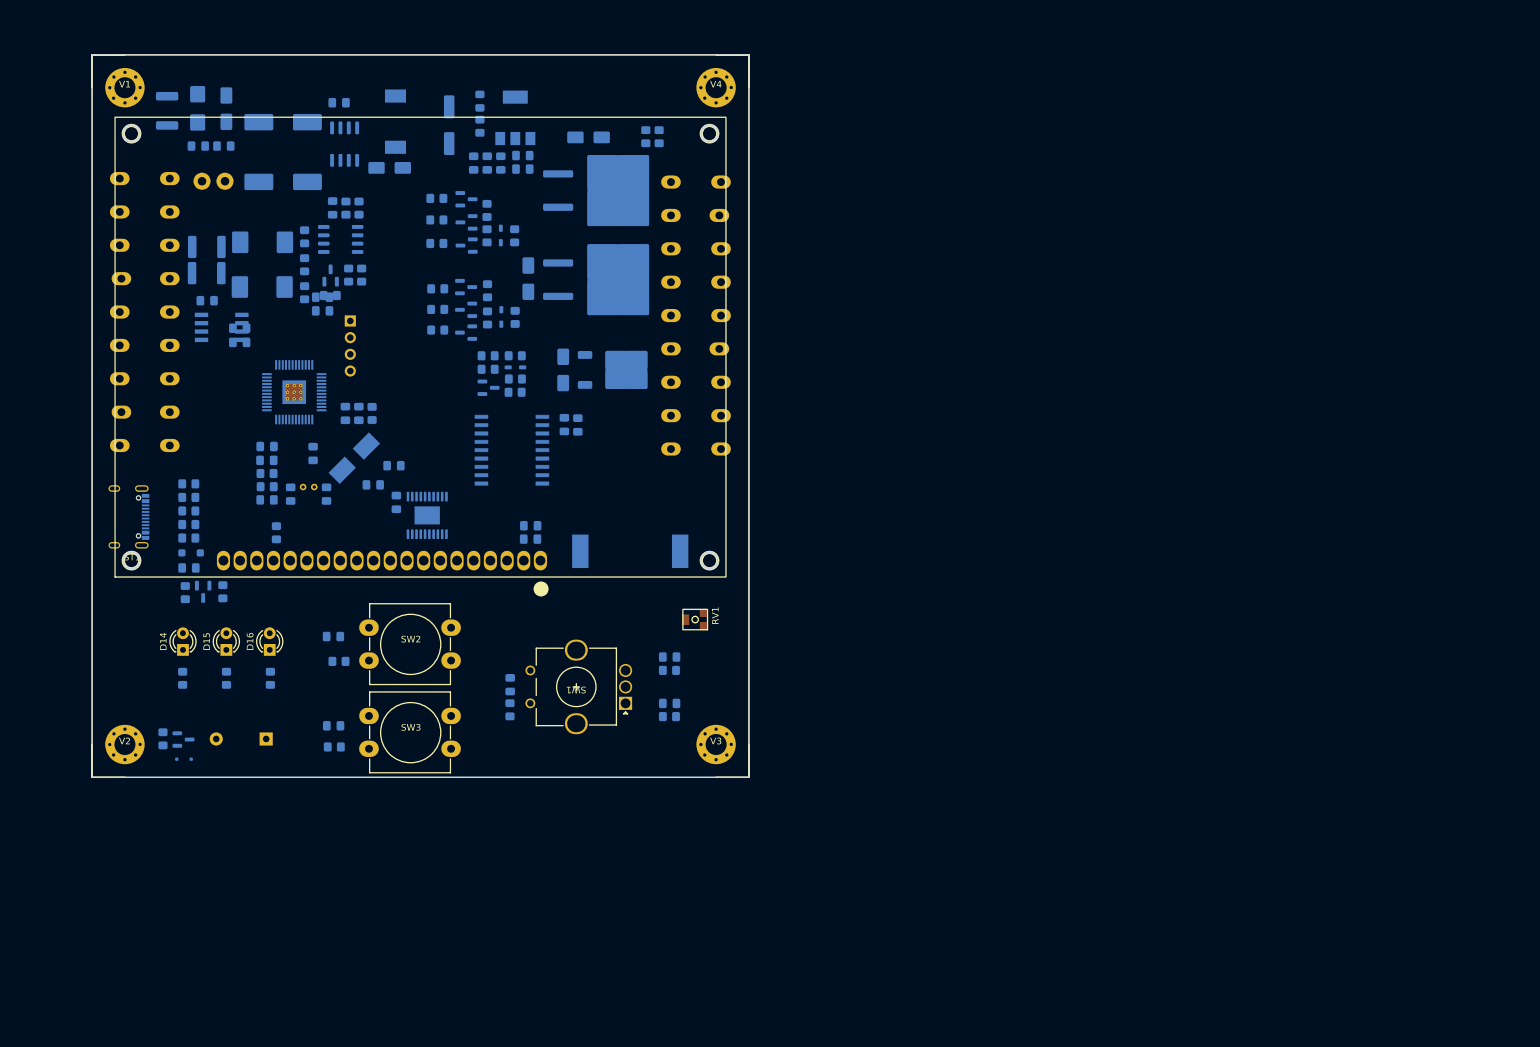
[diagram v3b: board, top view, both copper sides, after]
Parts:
- removed the D6 at (81.8, 51.3)
- removed the D8 at (239.3, 41.6)
- removed the D9 at (81.8, 65.2)
- removed the Q2 at (81.6, 47.0)
- removed the Q4 at (82.4, 59.7)
- removed the Q8 at (254.8, 39.7)
- removed the Q9 at (254.8, 44.1)
- removed the R17 at (306.8, 72.5)
- removed the R18 at (306.8, 75.5)
- removed the R20 at (302.1, 54.8)
- removed the R22 at (302.1, 60.7)
- removed the R24 at (302.1, 66.6)
- removed the R26 at (85.1, 54.5)
- removed the R32 at (297.3, 63.7)
- removed the R33 at (297.3, 66.6)
- removed the R34 at (297.3, 69.6)
- removed the R35 at (297.3, 72.5)
- removed the R39 at (292.6, 57.8)
- removed the R41 at (292.6, 63.7)
- removed REF** (x4): Vit-4mm, nhantt-kicad-lib:Vit-4mm
- C35: value 220uF_50V -> 10uF; footprint Capacitor_SMD:CP_Elec_8x10.5 -> Capacitor_SMD:C_0805_2012Metric_Pad1.18x1.45mm_HandSolder; moved to B.Cu
- C36, C37, C38, D17, D8, LS1, Q10, Q11, Q12, Q2, Q4, Q9, R17, R18, R20, R22, R24, R26, R32, R33, R34, R35, R39, R41, R42, R43, R44, R45, R46, U6: moved to B.Cu
- D6, D9: footprint Diode_SMD:D_SMA -> Diode_SMD:D_SC-80_HandSoldering; moved to B.Cu
- moved R40 202.0 mm to (100.8, 124.1), turned to -90 degrees
- moved D14 179.0 mm to (103.8, 110.6), turned to 90 degrees
- moved Q7 175.2 mm to (103.9, 124.2), turned to 0 degrees
- moved D15 173.8 mm to (110.4, 110.6), turned to 90 degrees
- moved R34 170.5 mm to (103.8, 114.9), turned to -90 degrees
- moved D16 168.7 mm to (117.0, 110.6), turned to 90 degrees
- moved R41 168.6 mm to (142.5, 48.7), turned to 180 degrees
- moved R42 167.4 mm to (142.5, 41.9), turned to 180 degrees
- moved R43 167.2 mm to (142.5, 45.1), turned to 180 degrees
- moved R35 164.6 mm to (110.5, 114.9), turned to -90 degrees
- moved R44 163.9 mm to (150.1, 43.7), turned to -90 degrees
- moved R45 163.4 mm to (150.1, 47.5), turned to 90 degrees
- moved R46 162.1 mm to (154.3, 47.5), turned to -90 degrees
- moved R39 158.9 mm to (117.1, 114.9), turned to -90 degrees
- moved Q12 153.6 mm to (147.0, 45.5), turned to 180 degrees
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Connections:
- D17 pad 1: VIN -> +24V Servo
- D8 pad 1: VIN -> +24V Servo
- D8 pad 2: /PWM1_OUT -> /PWM_Heater
- F1 pad 1: VIN -> +24V Servo
- H1 pad 1: VIN -> +24V Servo
- H1 pad 5: GND -> /T+
- H1 pad 6: /T+ -> GND
- H1 pad 9: GND -> /PWM2_OUT
- Q8 pad 2: /PWM1_OUT -> /PWM_Heater
- R17 pad 2: /PWM1 -> /PWM_1
- R41 pad 2: /PWM2 -> /PWM_3
- U6 pad 11: /ULN_EXTRA_4 -> unconnected-(U6-O8-Pad11)
- U6 pad 12: /ULN_EXTRA_3 -> unconnected-(U6-O7-Pad12)
- U6 pad 4: /PWM_1 -> unconnected-(U6-I4-Pad4)
- U6 pad 7: unconnected-(U6-I7-Pad7) -> GND
- U6 pad 8: unconnected-(U6-I8-Pad8) -> GND
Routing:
- net (no net): vias 0 -> 4
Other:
- board size 100 x 100 mm -> 100 x 110 mm
